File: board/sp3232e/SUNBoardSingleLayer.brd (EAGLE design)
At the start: 101.6 x 53.3 mm, 25 parts

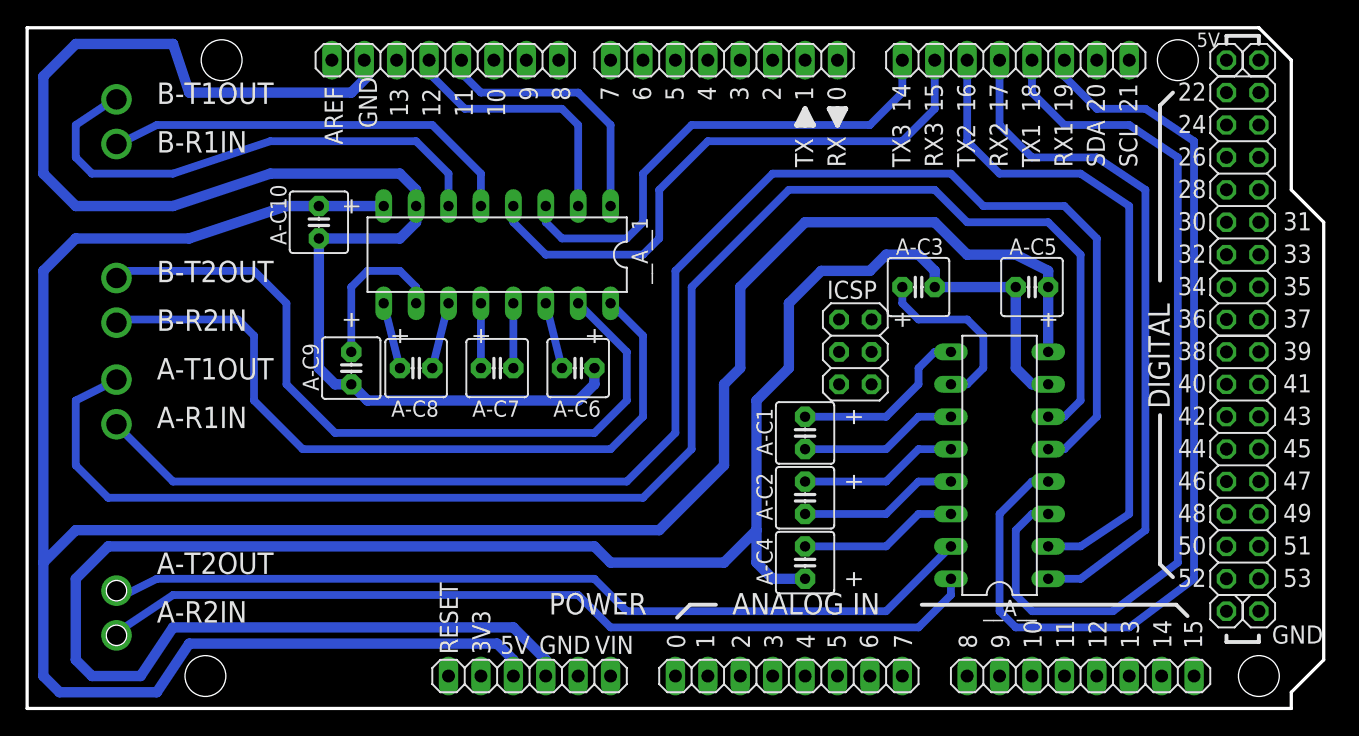
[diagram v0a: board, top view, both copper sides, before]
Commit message: Added 2 more pin to be compliant with more arduino and shields
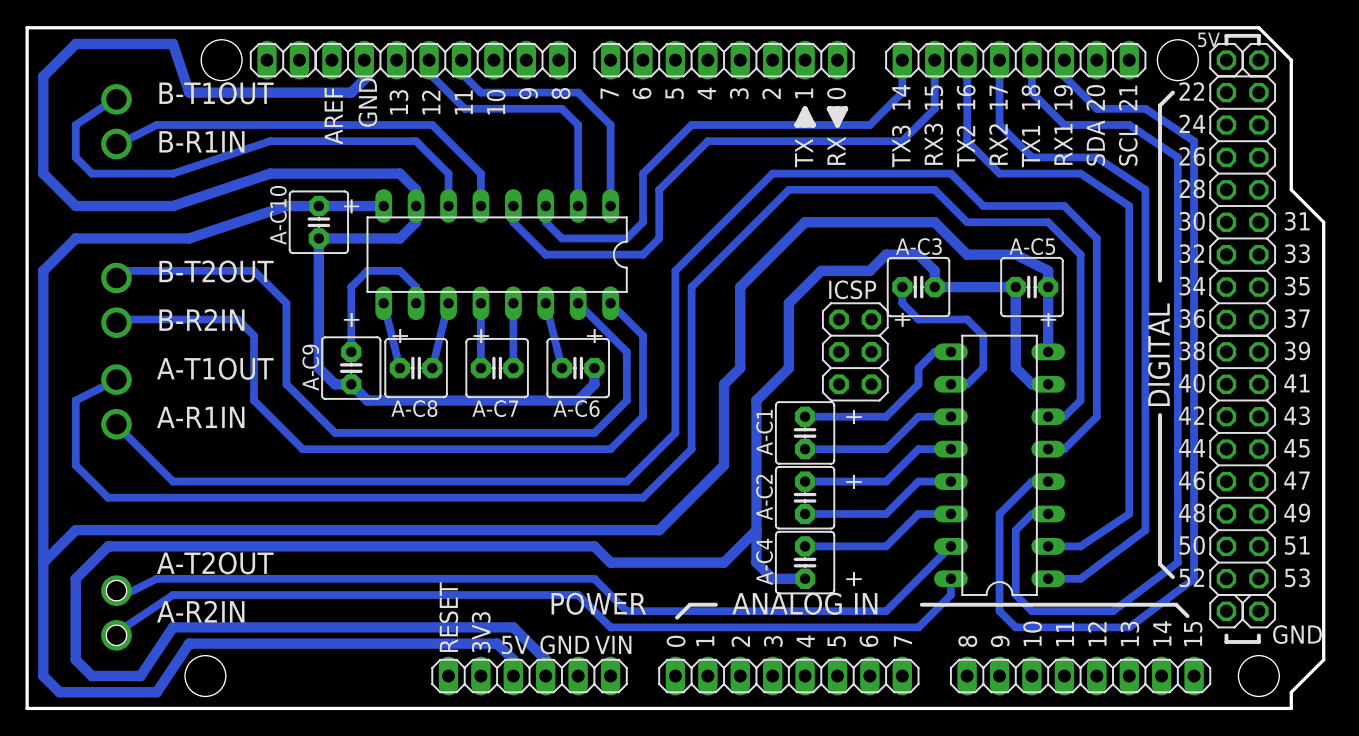
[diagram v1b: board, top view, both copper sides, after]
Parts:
- added SCL_SOA: (no value), pinhead:1X02
- renumbered __A__ to RS232-TO_TTL_A, __A__1 to RS232-TO-TTL_B
